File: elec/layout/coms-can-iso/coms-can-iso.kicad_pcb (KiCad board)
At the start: 2 copper layers, 15 parts, among them U10 60.4Ω ±1% 62.5mW, U11 60.4Ω ±1% 62.5mW, U12 1µF ±10% 25V X5R, U13 1µF ±10% 25V X5R, U2 1µF ±10% 25V X5R, U4 10pF ±5% 50V C0G, U5 10pF ±5% 50V C0G, U6 4.7µF ±10% 25V X5R, U7 10µF ±10% 25V X5R, U9 4.7nF ±10% 50V X7R

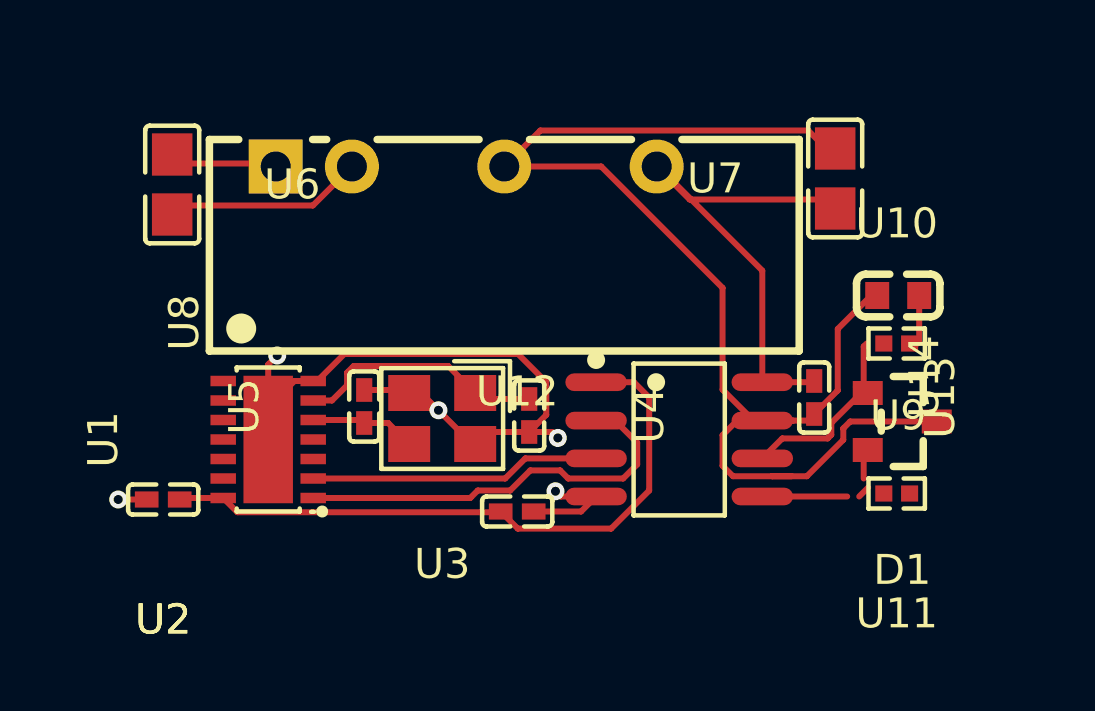
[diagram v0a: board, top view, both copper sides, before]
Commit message: update layouts to kicad 9
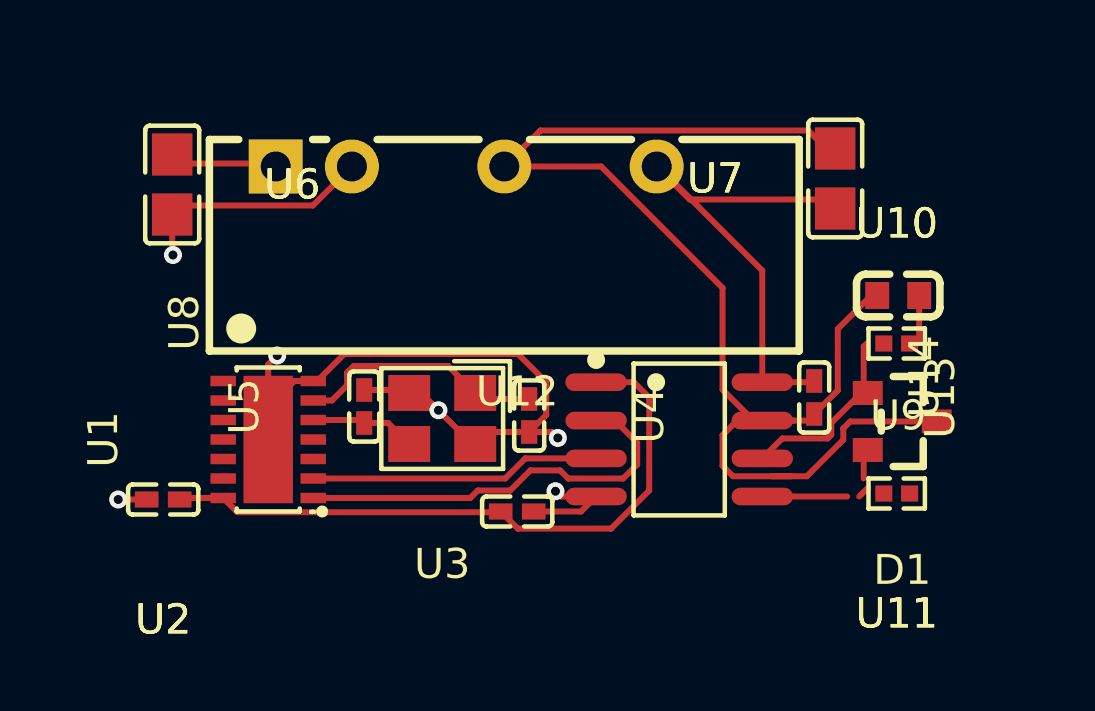
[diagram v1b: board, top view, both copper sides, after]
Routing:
- net gnd: track 34.8 -> 36.1 mm, vias 5 -> 6

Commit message: add power button and boot button, fix CAN layout
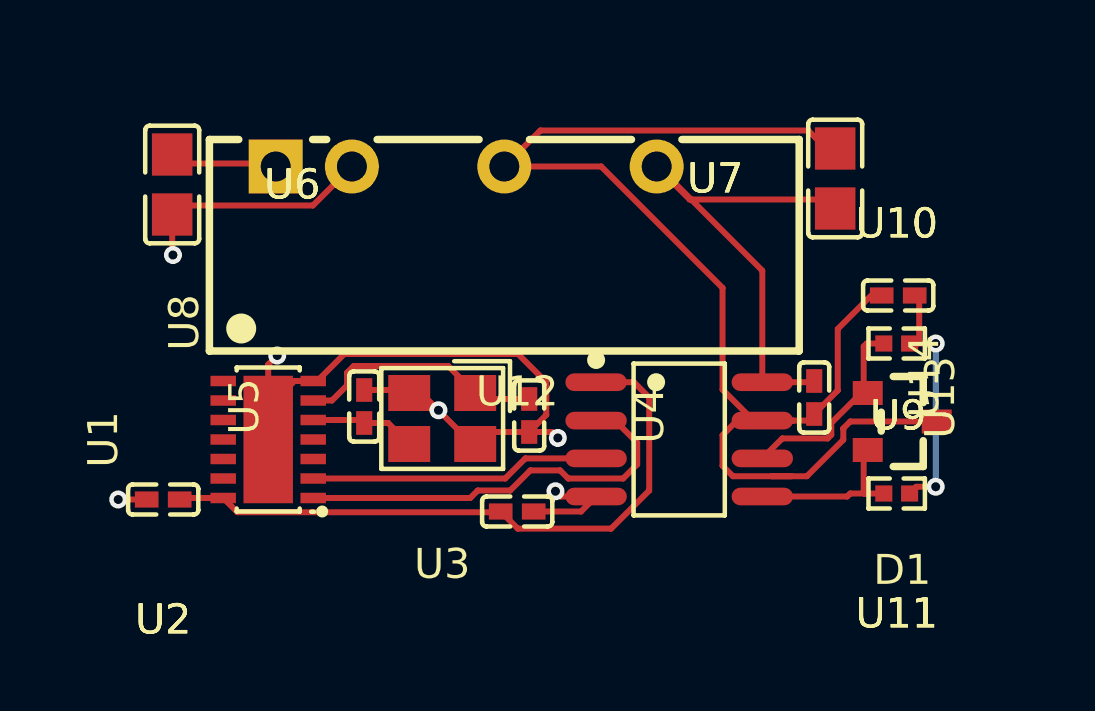
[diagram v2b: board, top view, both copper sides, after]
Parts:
- U9: footprint atopile:C0603-bd72f6 -> atopile:C0402-b3ef17
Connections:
- net controller-line-3 renamed INTh
- D1 pad 3: gnd-1 -> gnd
- U1 pad 10: line -> line-3
- U1 pad 11: line-3 -> line
- U1 pad 14: hv -> hv-1
- U1 pad 15: gnd -> gnd-1
- U1 pad 7: gnd -> gnd-1
- U1 pad 8: controller-line-2 -> controller-line-1
- U1 pad 9: controller-line-1 -> INT0h_GPIO0_XSTBY
- U12 pad 1: hv -> hv-1
- U12 pad 2: gnd -> gnd-1
- U13 pad 1: hv-1 -> hv-2
- U13 pad 2: gnd-1 -> gnd
- U14 pad 1: hv -> hv-1
- U14 pad 4: gnd -> gnd-1
- U14 pad 7: gnd-1 -> gnd
- U14 pad 8: hv-1 -> hv-2
- U2 pad 1: hv -> hv-1
- U2 pad 2: gnd -> gnd-1
- U3 pad 2: gnd -> gnd-1
- U3 pad 4: gnd -> gnd-1
- U4 pad 2: gnd -> gnd-1
- U5 pad 2: gnd -> gnd-1
- U6 pad 1: hv-2 -> hv
- U6 pad 2: gnd -> gnd-1
- U7 pad 1: hv-1 -> hv-2
- U7 pad 2: gnd-1 -> gnd
- U8 pad 1: hv-2 -> hv
- U8 pad 2: gnd -> gnd-1
- U8 pad 4: gnd-1 -> gnd
- U8 pad 6: hv-1 -> hv-2
- U9 pad 2: gnd-1 -> gnd
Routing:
- net hv: track 21.7 -> 3.49 mm
- net hv-2: track 3.49 -> 16.7 mm
- net gnd-1: track 45.0 -> 36.1 mm, vias 0 -> 6
- net gnd: track 36.1 -> 45.0 mm, vias 6 -> 0
- net _midpoint: track 1.62 -> 8.23 mm, vias 0 -> 2
- net hv-1: track 16.7 -> 21.7 mm
- net CANL: track 4.55 -> 5.89 mm
- net CANH: track 7.34 -> 7.91 mm

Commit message: Add isolation cut in CAN coms, route traces for proper clearance
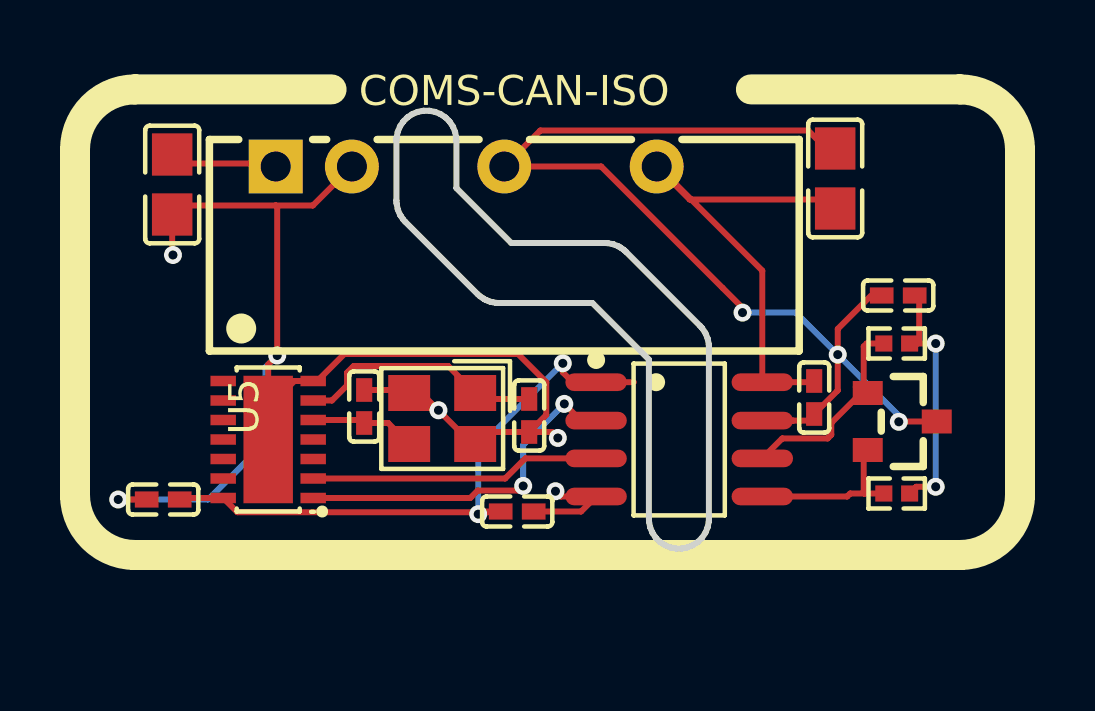
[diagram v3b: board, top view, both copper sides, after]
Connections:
- net controller-line renamed CLKO_SOF
- net controller-line-1 renamed INT1h_GPIO1
- net line renamed SDI
- net line-1 renamed SDO
- net line-2 renamed nCS
- net line-3 renamed SCK
- U1 pad 14: hv-1 -> hv
- U12 pad 1: hv-1 -> hv
- U13 pad 1: hv-2 -> hv-1
- U14 pad 1: hv-1 -> hv
- U14 pad 8: hv-2 -> hv-1
- U2 pad 1: hv-1 -> hv
- U6 pad 1: hv -> hv-2
- U7 pad 1: hv-2 -> hv-1
- U8 pad 1: hv -> hv-2
- U8 pad 6: hv-2 -> hv-1
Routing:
- net hv: track 3.49 -> 20.7 mm, vias 0 -> 2
- net gnd-1: track 36.1 -> 49.9 mm
- net hv-2: track 16.7 -> 3.49 mm
- net gnd: track 45.0 -> 38.7 mm, vias 0 -> 3
- net hv-1: track 21.7 -> 16.7 mm
- net tx: track 13.9 -> 12.4 mm, vias 0 -> 2
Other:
- board outline added: 10.4 x 14.6 mm
- board text added: "COMS-CAN-ISO"

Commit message: add isolation rating marking
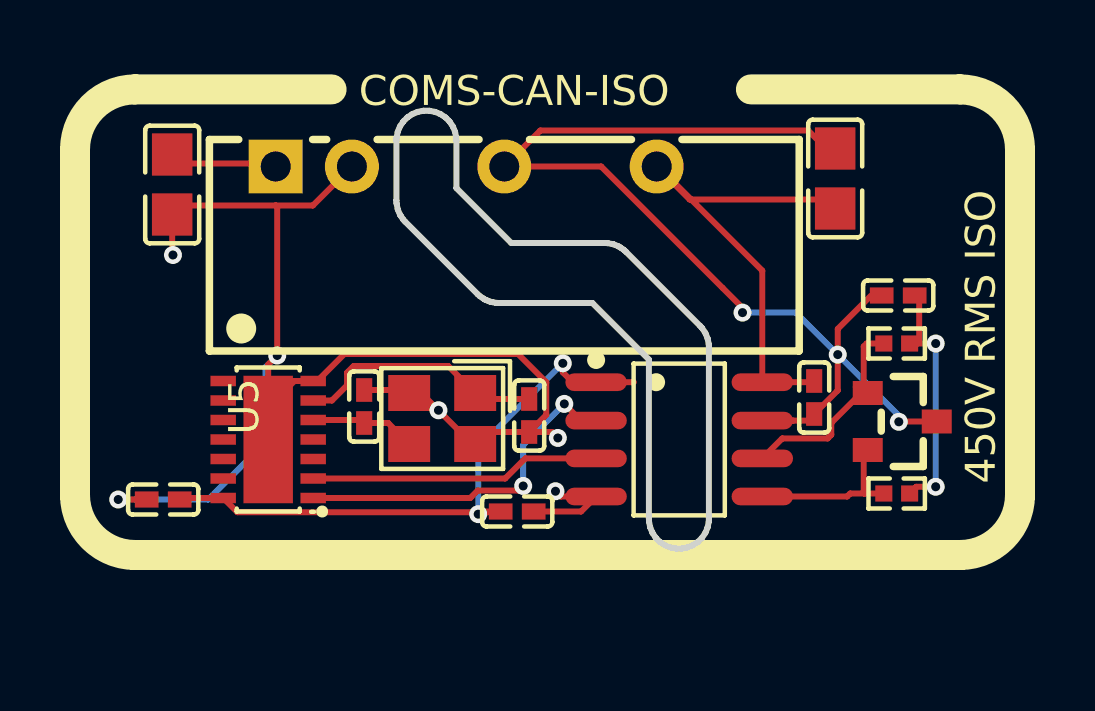
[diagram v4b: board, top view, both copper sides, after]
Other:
- board text added: "450V RMS ISO"
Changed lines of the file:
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@@
 		(layer "Edge.Cuts")
+	)
+	(gr_text "450V RMS ISO"
+		(at 158.74 77.67 90)
+		(layer "F.SilkS")
+		(effects
+			(font
+				(size 1 1)
+				(thickness 0.1)
+			)
+			(justify left bottom)
+		)
 	)
 	(gr_text "COMS-CAN-ISO"

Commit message: tidy up isolated supplies
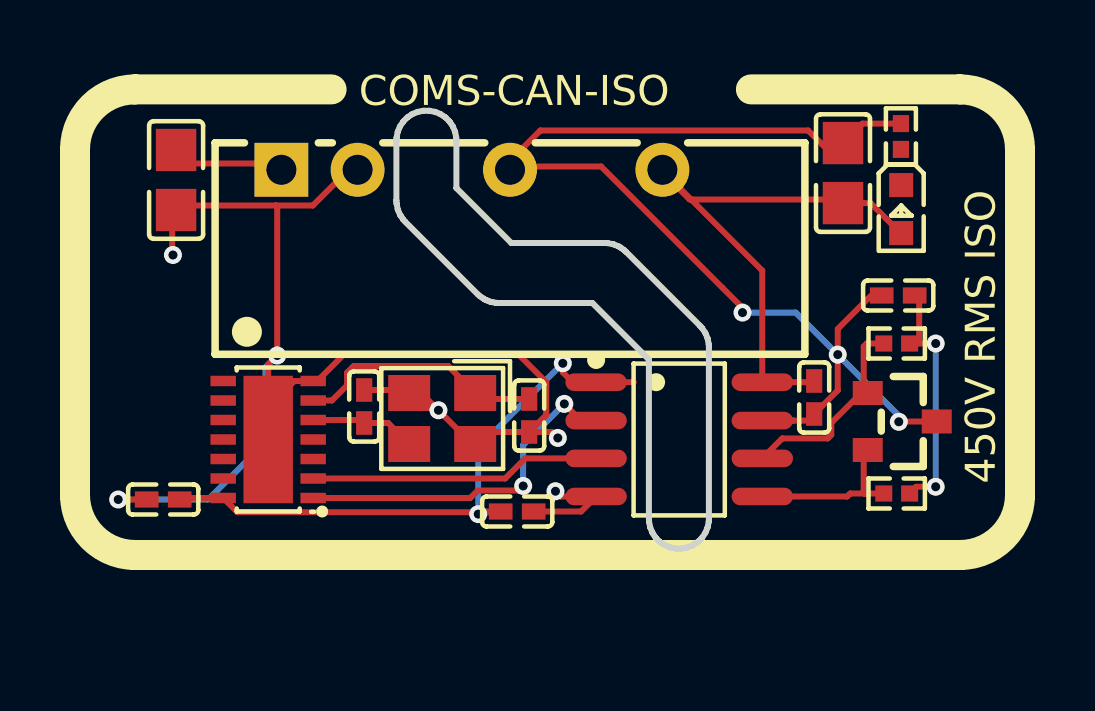
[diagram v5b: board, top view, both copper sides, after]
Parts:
- removed U7: 10µF ±10% 25V X5R, atopile:C0805-3b2e55
- removed U8: , atopile:PWRM-TH_BXXXXS-2WR3-d8b2fb
- added C1: 2.2µF ±10% 25V X7R, atopile:C0805-3b2e55, F.Cu at (131.3, 67.5)
- added C2: 10µF ±10% 25V X5R, atopile:C0805-3b2e55, F.Cu at (153.6, 67.3)
- added D2: , atopile:LED0603-RD-c81ffb, F.Cu at (155.5, 68.5)
- added R1: 1kΩ ±1% 62.5mW, atopile:R0402-56259e, F.Cu at (155.5, 66.1)
- U6: value 4.7µF ±10% 25V X5R -> (none); footprint atopile:C0805-3b2e55 -> atopile:PWRM-TH_BXXXXS-2WR3-d8b2fb
- moved U6 10.0 mm to (141.2, 67.2), turned to 0 degrees
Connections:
- U13 pad 1: hv-1 -> hv-2
- U14 pad 8: hv-1 -> hv-2
- U6 pad 1: hv-2 -> hv-1
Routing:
- net hv-2: track 3.49 -> 19.0 mm
- net hv-1: track 16.7 -> 3.49 mm
- net gnd: track 38.7 -> 40.9 mm

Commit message: building frozen
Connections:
- C1 pad 1: hv-1 -> hv-2
- C1 pad 2: gnd-1 -> gnd
- C2 pad 1: hv-2 -> hv
- C2 pad 2: gnd -> gnd-1
- D1 pad 3: gnd -> gnd-1
- D2 pad 2: hv-2 -> hv
- R1 pad 2: gnd -> gnd-1
- U1 pad 14: hv -> hv-1
- U1 pad 15: gnd-1 -> gnd
- U1 pad 7: gnd-1 -> gnd
- U12 pad 1: hv -> hv-1
- U12 pad 2: gnd-1 -> gnd
- U13 pad 1: hv-2 -> hv
- U13 pad 2: gnd -> gnd-1
- U14 pad 1: hv -> hv-1
- U14 pad 4: gnd-1 -> gnd
- U14 pad 7: gnd -> gnd-1
- U14 pad 8: hv-2 -> hv
- U2 pad 1: hv -> hv-1
- U2 pad 2: gnd-1 -> gnd
- U3 pad 2: gnd-1 -> gnd
- U3 pad 4: gnd-1 -> gnd
- U4 pad 2: gnd-1 -> gnd
- U5 pad 2: gnd-1 -> gnd
- U6 pad 1: hv-1 -> hv-2
- U6 pad 2: gnd-1 -> gnd
- U6 pad 4: gnd -> gnd-1
- U6 pad 6: hv-2 -> hv
- U9 pad 2: gnd -> gnd-1
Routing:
- net hv-1: track 3.49 -> 20.7 mm, vias 0 -> 2
- net hv-2: track 19.0 -> 3.49 mm
- net gnd-1: track 49.9 -> 40.9 mm, vias 6 -> 3
- net gnd: track 40.9 -> 49.9 mm, vias 3 -> 6
- net hv: track 20.7 -> 19.0 mm, vias 2 -> 0

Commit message: Build everything with ordered params to fix frozen builds
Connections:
- C1 pad 1: hv-2 -> hv-1
- C2 pad 1: hv -> hv-2
- D2 pad 2: hv -> hv-2
- U1 pad 14: hv-1 -> hv
- U12 pad 1: hv-1 -> hv
- U13 pad 1: hv -> hv-2
- U14 pad 1: hv-1 -> hv
- U14 pad 8: hv -> hv-2
- U2 pad 1: hv-1 -> hv
- U6 pad 1: hv-2 -> hv-1
- U6 pad 6: hv -> hv-2
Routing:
- net hv-1: track 20.7 -> 3.49 mm, vias 2 -> 0
- net hv-2: track 3.49 -> 19.0 mm
- net hv: track 19.0 -> 20.7 mm, vias 0 -> 2

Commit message: Cleanup layout for usb hub and usb-uart, add CM5 controller heatsink outline
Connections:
- C1 pad 1: hv-1 -> hv
- U1 pad 14: hv -> hv-1
- U12 pad 1: hv -> hv-1
- U14 pad 1: hv -> hv-1
- U2 pad 1: hv -> hv-1
- U6 pad 1: hv-1 -> hv
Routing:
- net hv-1: track 3.49 -> 20.7 mm, vias 0 -> 2
- net hv: track 20.7 -> 3.49 mm, vias 2 -> 0
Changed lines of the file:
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@@
     (net 14 "rx")
     (net 15 "xin")
-    (net 16 "hv")
+    (net 16 "hv-1")
     (net 17 "gnd")
     (net 18 "cathode")
     (net 19 "gnd-1")
-    (net 20 "hv-1")
+    (net 20 "hv")
     (net 21 "hv-2")
     (footprint "atopile:C0402-b3ef17"
@@
             (drill 0.999998)
             (layers "*.Cu" "*.Mask")
-            (net 20 "hv-1")
+            (net 20 "hv")
             (remove_unused_layers no)
         )
@@
             (size 0.59 2.05)
             (layers "F.Cu" "F.Mask" "F.Paste")
-            (net 16 "hv")
+            (net 16 "hv-1")
         )
         (pad "2" smd oval
@@
             (size 0.79 0.54)
             (layers "F.Cu" "F.Mask" "F.Paste")
-            (net 16 "hv")
+            (net 16 "hv-1")
         )
         (pad "2" smd rect
@@
             (size 0.79 0.54)
             (layers "F.Cu" "F.Mask" "F.Paste")
-            (net 16 "hv")
+            (net 16 "hv-1")
         )
         (pad "2" smd rect
@@
             (size 1.41 1.35)
             (layers "F.Cu" "F.Mask" "F.Paste")
-            (net 20 "hv-1")
+            (net 20 "hv")
         )
         (pad "2" smd rect
@@
             (size 0.85 0.35)
             (layers "F.Cu" "F.Mask" "F.Paste")
-            (net 16 "hv")
+            (net 16 "hv-1")
         )
         (pad "15" smd rect
